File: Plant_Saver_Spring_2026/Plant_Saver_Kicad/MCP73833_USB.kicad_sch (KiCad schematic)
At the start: 8 parts, among them U17 MCP73833-xxx-UN

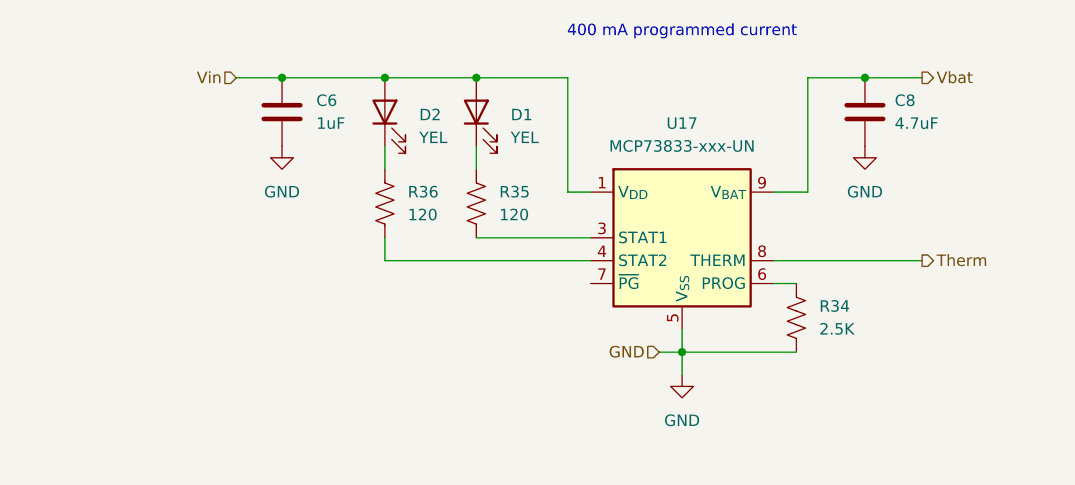
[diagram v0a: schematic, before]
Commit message: Updates to power schematic
Replaced certain selection transistors for lower Rds_on, added thermal cutoff and DW03 for battery protection, swapped in 4-channel op-amps for solar measurement, various misc. improvements.
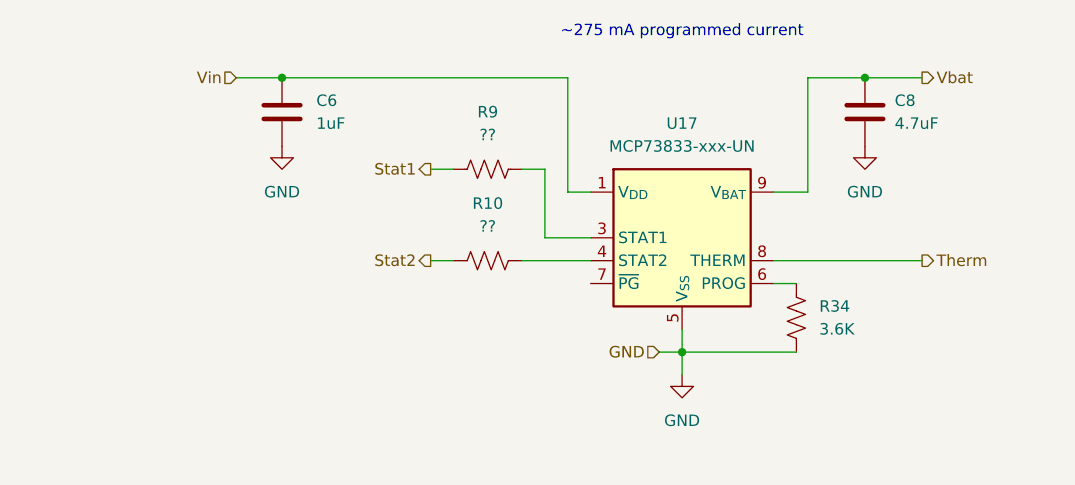
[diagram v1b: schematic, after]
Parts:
- removed D1, D2: YEL, LED_SMD:LED_1206_3216Metric, symbol Device:LED
- removed R35, R36: 120, Resistor_THT:R_Axial_DIN0207_L6.3mm_D2.5mm_P10.16mm_Horizontal, symbol Device:R_US
- added R10, R9: ??, Resistor_THT:R_Axial_DIN0207_L6.3mm_D2.5mm_P10.16mm_Horizontal, symbol Device:R_US
- C6: footprint (none) -> C410C105K5R5TA7200:CAP_C410C_AX_X7R_AXIMAX_KEM
- R34: value 2.5K -> 3.6K
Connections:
- net at U17.3 (STAT1): now also R9.2
- net at U17.4 (STAT2): now also R10.2
- new net Stat1: R9.1
- new net Stat2: R10.1
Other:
- note added: "~275 mA programmed current"
- note removed: "400 mA programmed current"

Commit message: Schematic updates
Added USB charge LEDs, updated PMOS gates, added micro connections and revised some of the charging set up.
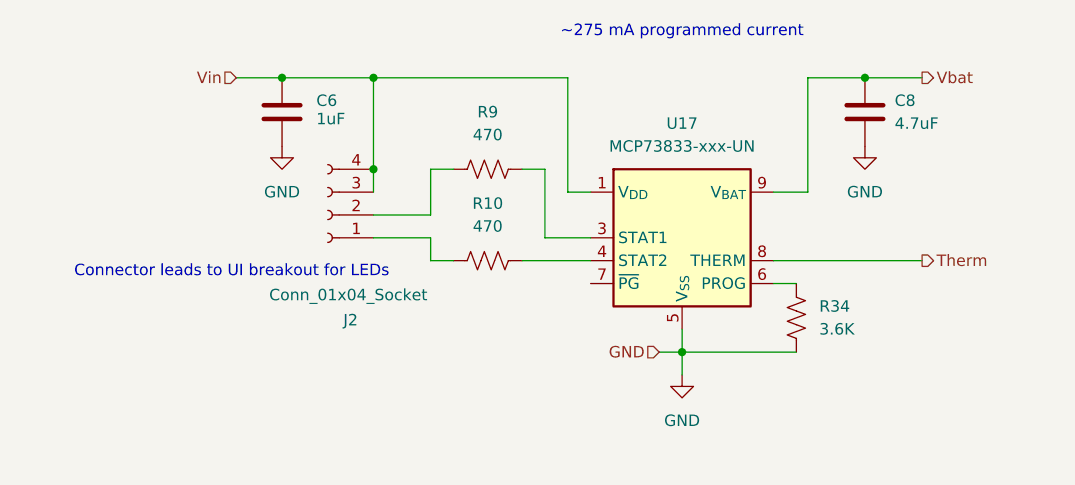
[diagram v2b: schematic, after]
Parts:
- added J2: Conn_01x04_Socket, symbol Connector:Conn_01x04_Socket
- R10, R9: value ?? -> 470
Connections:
- net Vin: now also J2.3 (Pin_3), J2.4 (Pin_4)
- net Stat1: no longer names the net of R9.1
- net Stat1: now also J2.2 (Pin_2)
- net Stat2: no longer names the net of R10.1
- net Stat2: now also J2.1 (Pin_1)
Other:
- note added: "Connector leads to UI breakout for LEDs"
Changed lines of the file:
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@@
 	(generator_version "9.0")
 	(paper "A4")
+	(text "Connector leads to UI breakout for LEDs\n"
+		(exclude_from_sim no)
+		(at 94.742 102.87 0)
+		(effects
+			(font
+				(size 1.27 1.27)
+			)
+		)
+	)
 	(text "~275 mA programmed current"
 		(exclude_from_sim no)
@@
 	)
 	(junction
+		(at 110.49 81.28)
+		(diameter 0)
+		(color 0 0 0 0)
+	)
+	(junction
 		(at 144.78 111.76)
+		(diameter 0)
+		(color 0 0 0 0)
+	)
+	(junction
+		(at 110.49 91.44)
 		(diameter 0)
 		(color 0 0 0 0)
@@
 	(wire
 		(pts
+			(xy 110.49 96.52) (xy 116.84 96.52)
+		)
+		(stroke
+			(width 0)
+			(type default)
+		)
+	)
+	(wire
+		(pts
 			(xy 129.54 91.44) (xy 127 91.44)
 		)
@@
 	(wire
 		(pts
+			(xy 110.49 81.28) (xy 132.08 81.28)
+		)
+		(stroke
+			(width 0)
+			(type default)
+		)
+	)
+	(wire
+		(pts
 			(xy 158.75 81.28) (xy 165.1 81.28)
 		)
@@
 	(wire
 		(pts
-			(xy 100.33 81.28) (xy 132.08 81.28)
+			(xy 100.33 81.28) (xy 110.49 81.28)
 		)
 		(stroke
@@
 	(wire
 		(pts
+			(xy 116.84 96.52) (xy 116.84 91.44)
+		)
+		(stroke
+			(width 0)
+			(type default)
+		)
+	)
+	(wire
+		(pts
 			(xy 144.78 109.22) (xy 144.78 111.76)
 		)
@@
 	(wire
 		(pts
+			(xy 110.49 99.06) (xy 116.84 99.06)
+		)
+		(stroke
+			(width 0)
+			(type default)
+		)
+	)
+	(wire
+		(pts
 			(xy 158.75 81.28) (xy 158.75 93.98)
 		)
@@
 	(wire
 		(pts
+			(xy 110.49 91.44) (xy 110.49 93.98)
+		)
+		(stroke
+			(width 0)
+			(type default)
+		)
+	)
+	(wire
+		(pts
+			(xy 110.49 81.28) (xy 110.49 91.44)
+		)
+		(stroke
+			(width 0)
+			(type default)
+		)
+	)
+	(wire
+		(pts
 			(xy 129.54 99.06) (xy 134.62 99.06)
 		)
@@
 	(wire
 		(pts
+			(xy 116.84 99.06) (xy 116.84 101.6)
+		)
+		(stroke
+			(width 0)
+			(type default)
+		)
+	)
+	(wire
+		(pts
 			(xy 129.54 91.44) (xy 129.54 99.06)
 		)
@@
 			(width 0)
 			(type default)
-		)
-	)
-	(hierarchical_label "Stat1"
-		(shape output)
-		(at 116.84 91.44 180)
-		(effects
-			(font
-				(size 1.27 1.27)
-			)
-			(justify right)
 		)
 	)
@@
 		)
 	)
-	(hierarchical_label "Stat2"
-		(shape output)
-		(at 116.84 101.6 180)
-		(effects
-			(font
-				(size 1.27 1.27)
-			)
-			(justify right)
-		)
-	)
 	(symbol
 		(lib_id "power:GND")
@@
 			)
 		)
-		(property "Value" "??"
+		(property "Value" "470"
 			(at 123.19 87.63 90)
 			(effects
@@
 				(path "/7f244634-d37a-4ff0-ba36-8027330ab1bd/c1b5c94f-5fb5-4e2b-895b-5d171c372d7d/8fec44fe-3d91-4aaf-a03f-f618b2e9c693"
 					(reference "R9")
+					(unit 1)
+				)
+			)
+		)
+	)
+	(symbol
+		(lib_id "Connector:Conn_01x04_Socket")
+		(at 105.41 96.52 180)
+		(unit 1)
+		(exclude_from_sim no)
+		(in_bom yes)
+		(on_board yes)
+		(dnp no)
+		(property "Reference" "J2"
+			(at 107.95 108.204 0)
+			(effects
+				(font
+					(size 1.27 1.27)
+				)
+			)
+		)
+		(property "Value" "Conn_01x04_Socket"
+			(at 107.696 105.41 0)
+			(effects
+				(font
+					(size 1.27 1.27)
+				)
+			)
+		)
+		(property "Footprint" ""
+			(at 105.41 96.52 0)
+			(effects
+				(font
+					(size 1.27 1.27)
+				)
+				(hide yes)
+			)
+		)
+		(property "Datasheet" "~"
+			(at 105.41 96.52 0)
+			(effects
+				(font
+					(size 1.27 1.27)
+				)
+				(hide yes)
+			)
+		)
+		(property "Description" "Generic connector, single row, 01x04, script generated"
+			(at 105.41 96.52 0)
+			(effects
+				(font
+					(size 1.27 1.27)
+				)
+				(hide yes)
+			)
+		)
+		(pin "1"
+		)
+		(pin "4"
+		)
+		(pin "2"
+		)
+		(pin "3"
+		)
+		(instances
+			(project ""
+				(path "/7f244634-d37a-4ff0-ba36-8027330ab1bd/c1b5c94f-5fb5-4e2b-895b-5d171c372d7d/8fec44fe-3d91-4aaf-a03f-f618b2e9c693"
+					(reference "J2")
 					(unit 1)
 				)
@@
 		(on_board yes)
 		(dnp no)
-		(fields_autoplaced yes)
 		(property "Reference" "C6"
 			(at 104.14 83.8199 0)
@@
 		)
 		(property "Value" "1uF"
-			(at 104.14 86.3599 0)
+			(at 104.14 85.852 0)
 			(effects
 				(font
@@
 			)
 		)
-		(property "Value" "??"
+		(property "Value" "470"
 			(at 123.19 97.79 90)
 			(effects

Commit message: Footprint correction
Changed the DHT20 from a header pin to the recommended SIP. Also had to reannotate in order to assign footprints.
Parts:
- renumbered C8 to C7, R9 to R27, R10 to R28, R34 to R35, U17 to U16
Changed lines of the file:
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@@
 		(dnp no)
 		(fields_autoplaced yes)
-		(property "Reference" "#PWR016"
+		(property "Reference" "#PWR027"
 			(at 100.33 95.25 0)
 			(effects
@@
 			(project "Plant_Saver_Kicad"
 				(path "/7f244634-d37a-4ff0-ba36-8027330ab1bd/c1b5c94f-5fb5-4e2b-895b-5d171c372d7d/8fec44fe-3d91-4aaf-a03f-f618b2e9c693"
-					(reference "#PWR016")
+					(reference "#PWR027")
 					(unit 1)
 				)
@@
 		(dnp no)
 		(fields_autoplaced yes)
-		(property "Reference" "#PWR023"
+		(property "Reference" "#PWR029"
 			(at 165.1 95.25 0)
 			(effects
@@
 			(project "Plant_Saver_Kicad"
 				(path "/7f244634-d37a-4ff0-ba36-8027330ab1bd/c1b5c94f-5fb5-4e2b-895b-5d171c372d7d/8fec44fe-3d91-4aaf-a03f-f618b2e9c693"
-					(reference "#PWR023")
+					(reference "#PWR029")
 					(unit 1)
 				)
@@
 		(dnp no)
 		(fields_autoplaced yes)
-		(property "Reference" "R9"
+		(property "Reference" "R27"
 			(at 123.19 85.09 90)
 			(effects
@@
 			(project "Plant_Saver_Kicad"
 				(path "/7f244634-d37a-4ff0-ba36-8027330ab1bd/c1b5c94f-5fb5-4e2b-895b-5d171c372d7d/8fec44fe-3d91-4aaf-a03f-f618b2e9c693"
-					(reference "R9")
+					(reference "R27")
 					(unit 1)
 				)
@@
 		(dnp no)
 		(fields_autoplaced yes)
-		(property "Reference" "R34"
+		(property "Reference" "R35"
 			(at 160.02 106.6799 0)
 			(effects
@@
 			(project "Plant_Saver_Kicad"
 				(path "/7f244634-d37a-4ff0-ba36-8027330ab1bd/c1b5c94f-5fb5-4e2b-895b-5d171c372d7d/8fec44fe-3d91-4aaf-a03f-f618b2e9c693"
-					(reference "R34")
+					(reference "R35")
 					(unit 1)
 				)
@@
 		(dnp no)
 		(fields_autoplaced yes)
-		(property "Reference" "U17"
+		(property "Reference" "U16"
 			(at 144.78 86.36 0)
 			(effects
@@
 			(project "Plant_Saver_Kicad"
 				(path "/7f244634-d37a-4ff0-ba36-8027330ab1bd/c1b5c94f-5fb5-4e2b-895b-5d171c372d7d/8fec44fe-3d91-4aaf-a03f-f618b2e9c693"
-					(reference "U17")
+					(reference "U16")
 					(unit 1)
 				)
@@
 		(dnp no)
 		(fields_autoplaced yes)
-		(property "Reference" "#PWR021"
+		(property "Reference" "#PWR028"
 			(at 144.78 120.65 0)
 			(effects
@@
 			(project "Plant_Saver_Kicad"
 				(path "/7f244634-d37a-4ff0-ba36-8027330ab1bd/c1b5c94f-5fb5-4e2b-895b-5d171c372d7d/8fec44fe-3d91-4aaf-a03f-f618b2e9c693"
-					(reference "#PWR021")
+					(reference "#PWR028")
 					(unit 1)
 				)
@@
 		(on_board yes)
 		(dnp no)
-		(property "Reference" "C8"
+		(property "Reference" "C7"
 			(at 168.402 83.82 0)
 			(effects
@@
 			(project "Plant_Saver_Kicad"
 				(path "/7f244634-d37a-4ff0-ba36-8027330ab1bd/c1b5c94f-5fb5-4e2b-895b-5d171c372d7d/8fec44fe-3d91-4aaf-a03f-f618b2e9c693"
-					(reference "C8")
+					(reference "C7")
 					(unit 1)
 				)
@@
 		(dnp no)
 		(fields_autoplaced yes)
-		(property "Reference" "R10"
+		(property "Reference" "R28"
 			(at 123.19 95.25 90)
 			(effects
@@
 			(project "Plant_Saver_Kicad"
 				(path "/7f244634-d37a-4ff0-ba36-8027330ab1bd/c1b5c94f-5fb5-4e2b-895b-5d171c372d7d/8fec44fe-3d91-4aaf-a03f-f618b2e9c693"
-					(reference "R10")
-					(unit 1)
-				)
+					(reference "R28")
+					(unit 1)
+				)

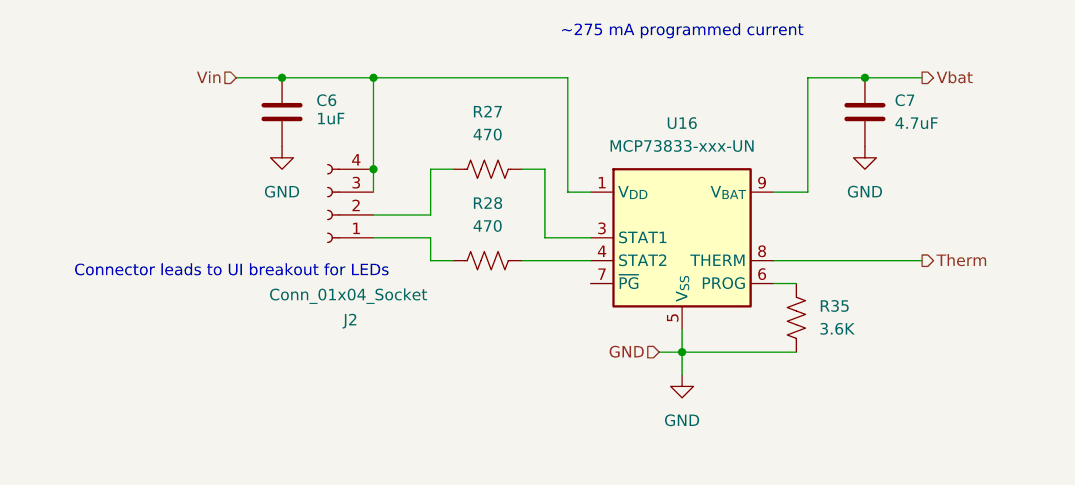
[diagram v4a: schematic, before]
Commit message: StripBoardTouchUp
Made everything on the stripboard go into connector pins that then integrate into the main sketch. Made Error LED go into pin 26 on the esp32.
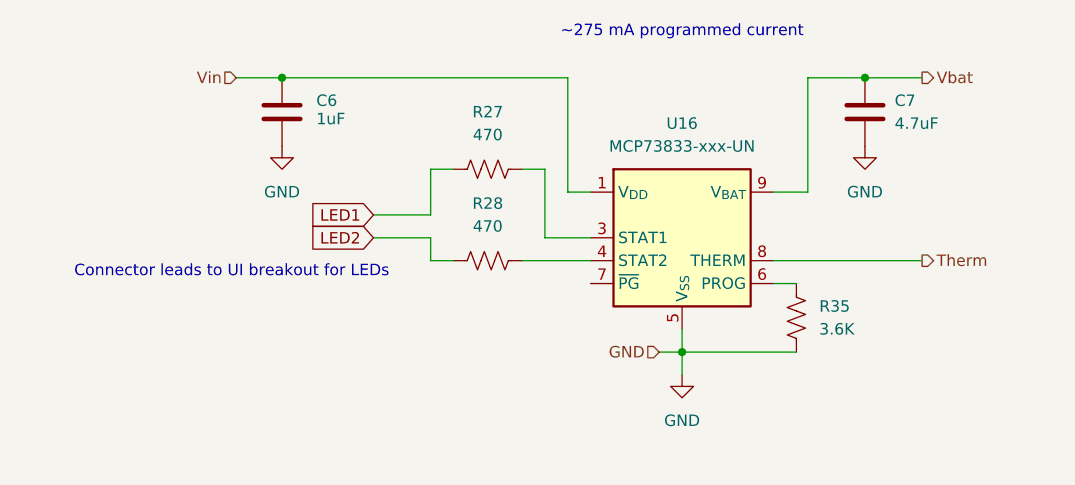
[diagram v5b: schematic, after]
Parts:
- removed J2: Conn_01x04_Socket, symbol Connector:Conn_01x04_Socket
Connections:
- net LED1: now reaches R27.1
- net LED2: now reaches R28.1
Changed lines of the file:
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@@
-	)
-	(junction
-		(at 110.49 81.28)
-		(diameter 0)
-		(color 0 0 0 0)
 	)
 	(junction
@@
 	)
 	(junction
-		(at 110.49 91.44)
-		(diameter 0)
-		(color 0 0 0 0)
-	)
-	(junction
 		(at 165.1 81.28)
 		(diameter 0)
@@
 	(wire
 		(pts
-			(xy 110.49 81.28) (xy 132.08 81.28)
-		)
-		(stroke
-			(width 0)
-			(type default)
-		)
-	)
-	(wire
-		(pts
 			(xy 158.75 81.28) (xy 165.1 81.28)
 		)
@@
 	(wire
 		(pts
-			(xy 100.33 81.28) (xy 110.49 81.28)
+			(xy 100.33 81.28) (xy 132.08 81.28)
 		)
 		(stroke
@@
 	(wire
 		(pts
-			(xy 110.49 91.44) (xy 110.49 93.98)
-		)
-		(stroke
-			(width 0)
-			(type default)
-		)
-	)
-	(wire
-		(pts
-			(xy 110.49 81.28) (xy 110.49 91.44)
-		)
-		(stroke
-			(width 0)
-			(type default)
-		)
-	)
-	(wire
-		(pts
 			(xy 129.54 99.06) (xy 134.62 99.06)
 		)
@@
 			(width 0)
 			(type default)
+		)
+	)
+	(global_label "LED1"
+		(shape input)
+		(at 110.49 96.52 180)
+		(fields_autoplaced yes)
+		(effects
+			(font
+				(size 1.27 1.27)
+			)
+			(justify right)
+		)
+		(property "Intersheetrefs" "${INTERSHEET_REFS}"
+			(at 102.8482 96.52 0)
+			(effects
+				(font
+					(size 1.27 1.27)
+				)
+				(justify right)
+				(hide yes)
+			)
+		)
+	)
+	(global_label "LED2"
+		(shape input)
+		(at 110.49 99.06 180)
+		(fields_autoplaced yes)
+		(effects
+			(font
+				(size 1.27 1.27)
+			)
+			(justify right)
+		)
+		(property "Intersheetrefs" "${INTERSHEET_REFS}"
+			(at 102.8482 99.06 0)
+			(effects
+				(font
+					(size 1.27 1.27)
+				)
+				(justify right)
+				(hide yes)
+			)
 		)
 	)
@@
 					(unit 1)
 				)
-			)
-		)
-	)
-	(symbol
-		(lib_id "Connector:Conn_01x04_Socket")
-		(at 105.41 96.52 180)
-		(unit 1)
-		(exclude_from_sim no)
-		(in_bom yes)
-		(on_board yes)
-		(dnp no)
-		(property "Reference" "J2"
-			(at 107.95 108.204 0)
-			(effects
-				(font
-					(size 1.27 1.27)
-				)
-			)
-		)
-		(property "Value" "Conn_01x04_Socket"
-			(at 107.696 105.41 0)
-			(effects
-				(font
-					(size 1.27 1.27)
-				)
-			)
-		)
-		(property "Footprint" ""
-			(at 105.41 96.52 0)
-			(effects
-				(font
-					(size 1.27 1.27)
-				)
-				(hide yes)
-			)
-		)
-		(property "Datasheet" "~"
-			(at 105.41 96.52 0)
-			(effects
-				(font
-					(size 1.27 1.27)
-				)
-				(hide yes)
-			)
-		)
-		(property "Description" "Generic connector, single row, 01x04, script generated"
-			(at 105.41 96.52 0)
-			(effects
-				(font
-					(size 1.27 1.27)
-				)
-				(hide yes)
-			)
-		)
-		(pin "1"
-		)
-		(pin "4"
-		)
-		(pin "2"
-		)
-		(pin "3"
-		)
-		(instances
-			(project "Charge_Circuit"
-				(path "/6972ab9f-ec90-4565-bd2c-bfb60d5a21f0/8fec44fe-3d91-4aaf-a03f-f618b2e9c693"
-					(reference "J2")
-					(unit 1)
-				)
-			)
-			(project ""
-				(path "/7f244634-d37a-4ff0-ba36-8027330ab1bd/c1b5c94f-5fb5-4e2b-895b-5d171c372d7d/8fec44fe-3d91-4aaf-a03f-f618b2e9c693"
-					(reference "J2")
-					(unit 1)
-				)

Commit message: Misc. changes
Updated peripheral power switch, UI board connections
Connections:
- net LED1 renamed STAT1
- net LED2 renamed STAT2
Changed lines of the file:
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@@
 		)
 	)
-	(global_label "LED1"
+	(global_label "STAT1"
 		(shape input)
 		(at 110.49 96.52 180)
@@
 		)
 		(property "Intersheetrefs" "${INTERSHEET_REFS}"
-			(at 102.8482 96.52 0)
+			(at 102.062 96.52 0)
 			(effects
 				(font
@@
 		)
 	)
-	(global_label "LED2"
+	(global_label "STAT2"
 		(shape input)
 		(at 110.49 99.06 180)
@@
 		)
 		(property "Intersheetrefs" "${INTERSHEET_REFS}"
-			(at 102.8482 99.06 0)
+			(at 102.062 99.06 0)
 			(effects
 				(font

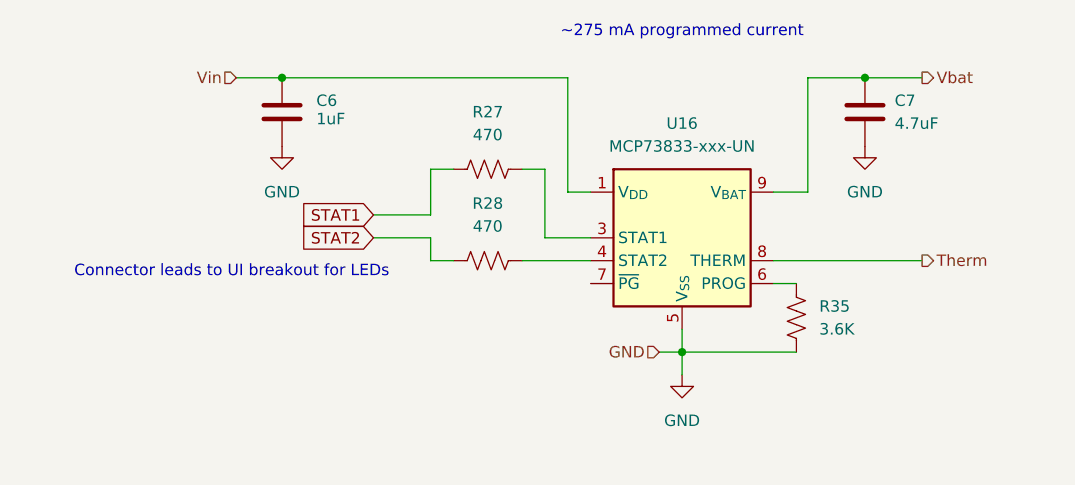
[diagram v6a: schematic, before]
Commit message: Footprint updates
Misc. schematic fixes, mostly updated/added footprints where needed.
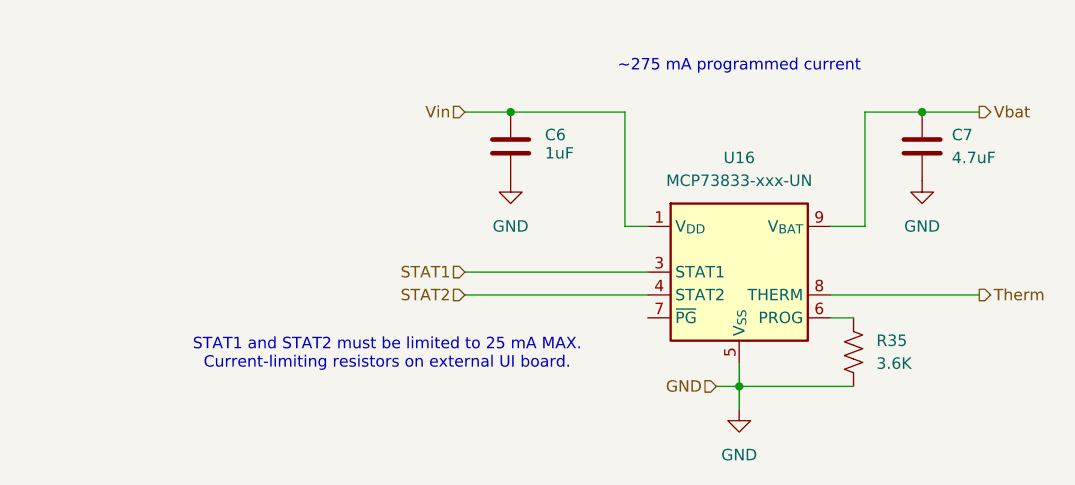
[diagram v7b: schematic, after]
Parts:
- removed R27, R28: 470, Resistor_THT:R_Axial_DIN0207_L6.3mm_D2.5mm_P10.16mm_Horizontal, symbol Device:R_US
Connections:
- net STAT1: now also U16.3 (STAT1)
- net STAT2: now also U16.4 (STAT2)
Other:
- note added: "STAT1 and STAT2 must be limited to 25 mA MAX. Current-limiting resistors on external UI board."
- note removed: "Connector leads to UI breakout for LEDs"
- moved on the sheet: C6, C7, R35, U16
